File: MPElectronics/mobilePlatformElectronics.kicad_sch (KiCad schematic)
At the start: 92 parts, among them J1 UART, J2 UART, J3 Magnetic Encoder, J4 Magnetic Encoder, M1 Motor_DC, M2 Motor_DC, M3 Motor_DC, M4 Motor_DC, M5 SG90 9g Micro Servo, M6 RDS51150, M7 RDS51150, M8 SY35ST28-0504A_Stepper_Motor_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, Q1 LTR3208E, SW1 Reset, SW2 Reset, SW3 Reset, SW4 SW_SPDT, SW5 SW_SPDT, SW6 SW_SPDT_LIMIT, SW7 SW_SPDT_LIMIT, U1 PIC32MX170F256B, U10 TLE5206-2S, U12 IR Distance, U13 IR Distance, U14 L293NE/SN754410NE, U2 TLE5206-2S, U3 PIC32MX170F256B, U4 IR Line Sensor, U5 IR Line Sensor, U6 IR Line Sensor, U7 MCP6294, U8 LM339AN, U9 IR Line Sensor

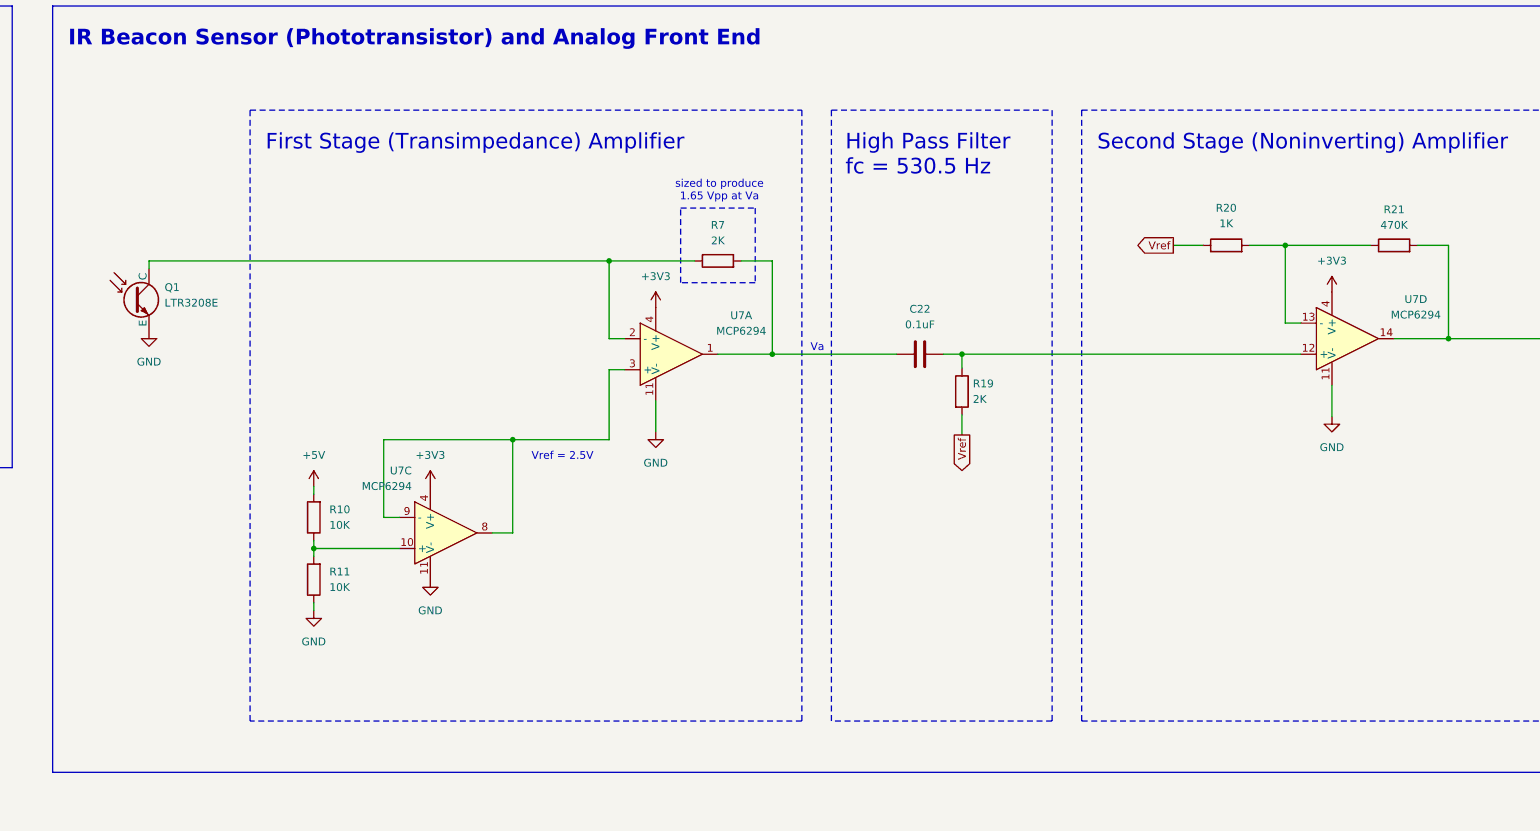
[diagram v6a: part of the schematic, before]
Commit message: changesignal conditioning vref connections and rails from 5v to 3v3
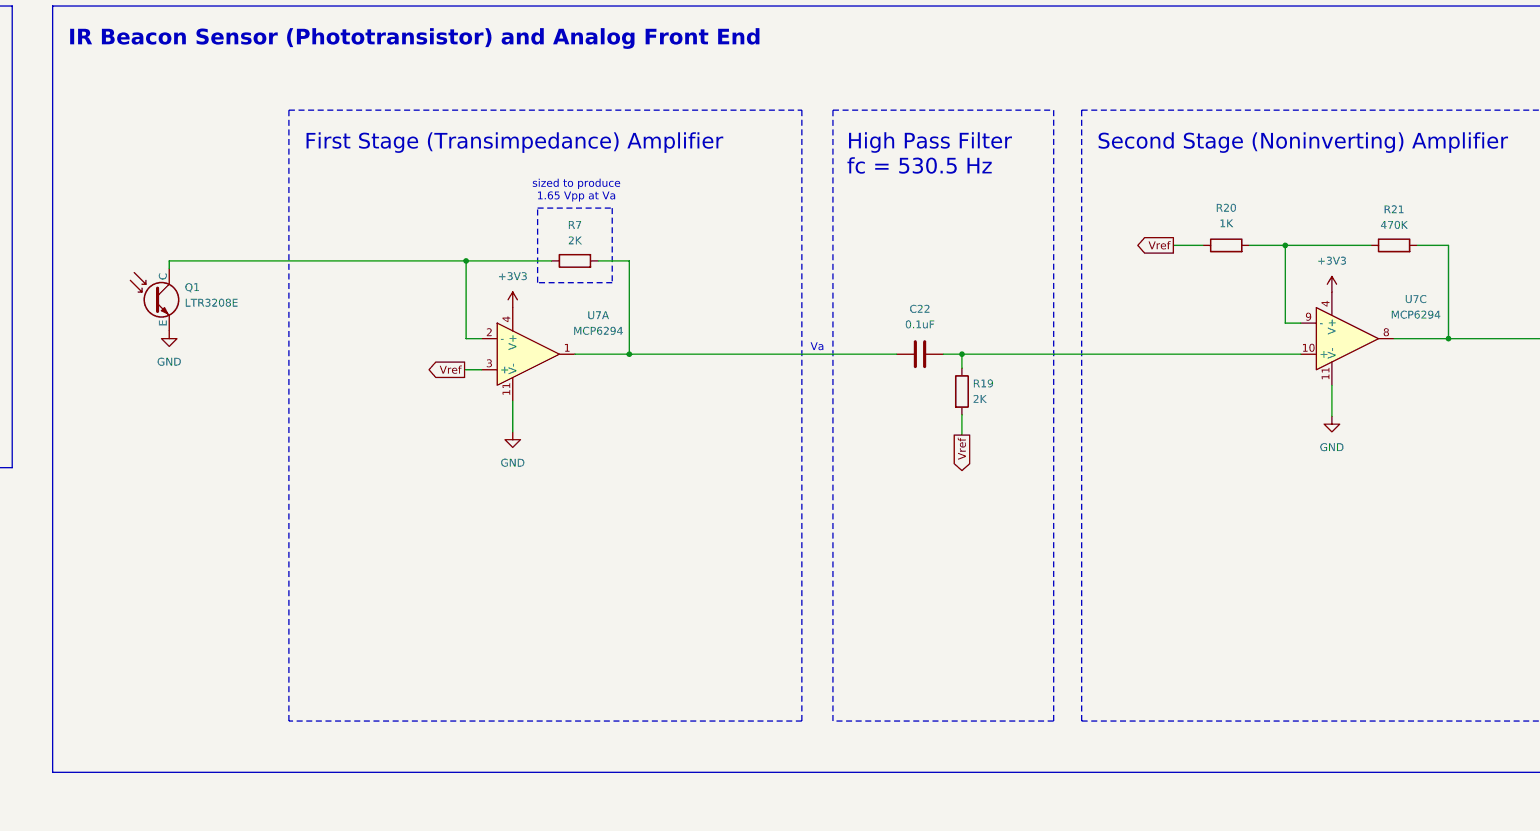
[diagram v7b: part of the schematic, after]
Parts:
- removed R10, R11: 10K, symbol ME218_BaseLib:Res2
- removed unit 3 of U7
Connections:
- net Vref: now also U7.3 (+)
- net at R20.2, R21.1: now also U7.9 (-); no longer U7.13 (-)
- net at R21.2, U8.4 (-): now also U7.8; no longer U7.14
- net at C22.1, R19.1: now also U7.10 (+); no longer U7.12 (+)
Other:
- note removed: "Vref = 2.5V"
- moved on the sheet: Q1, R7, U7A

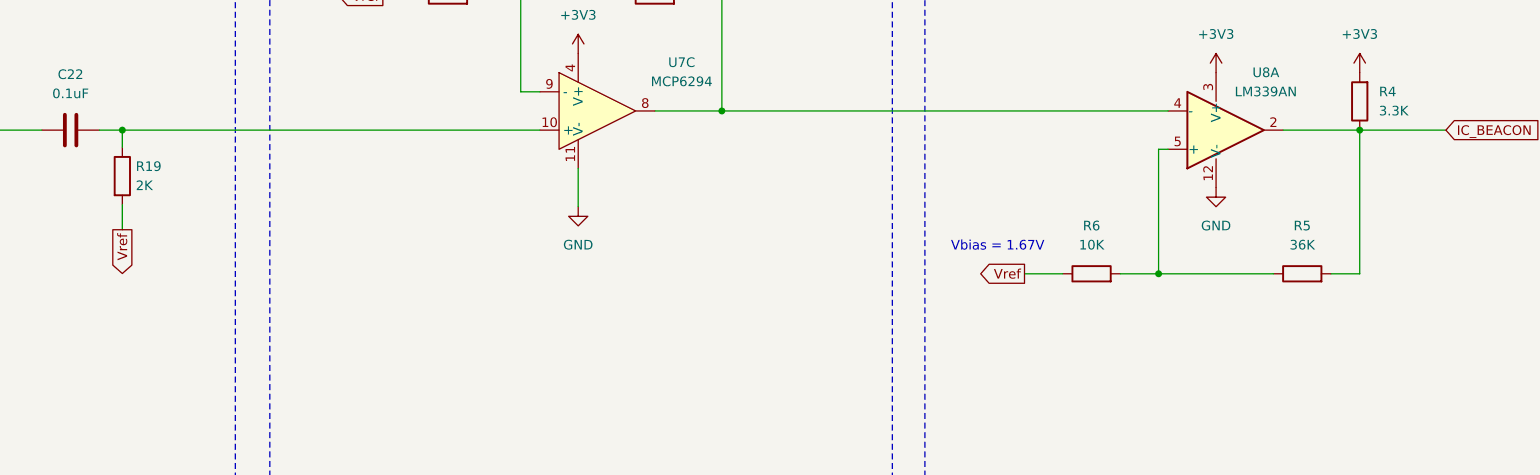
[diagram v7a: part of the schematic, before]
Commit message: schematic filter update
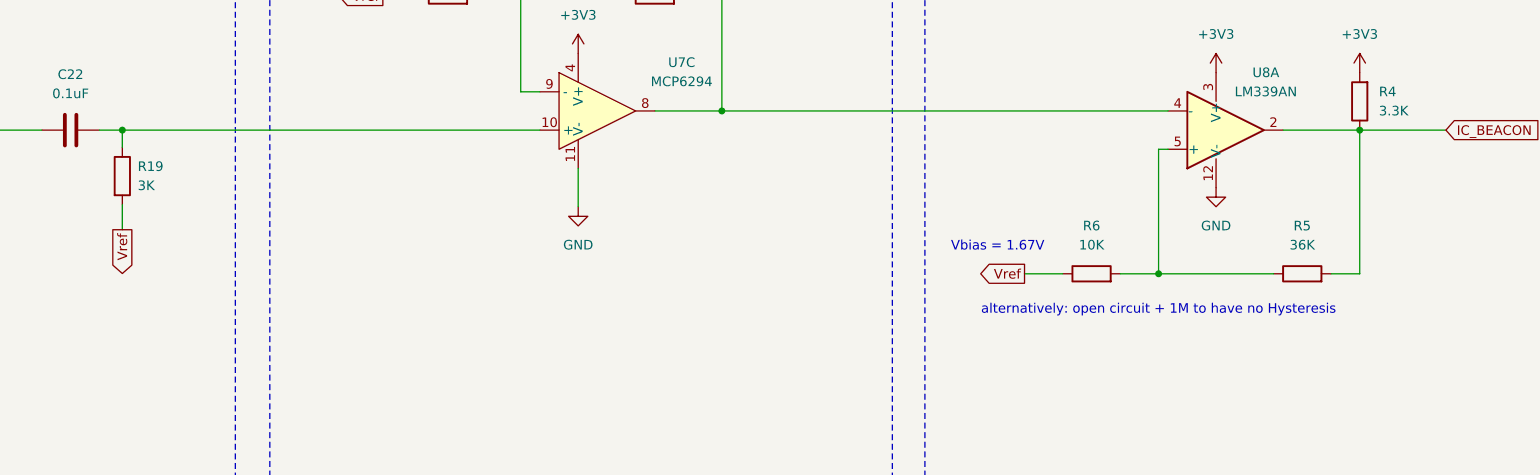
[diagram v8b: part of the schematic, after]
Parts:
- R19: value 2K -> 3K
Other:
- note added: "alternatively: open circuit + 1M to have no Hysteresis"
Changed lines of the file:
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@@
 		)
 	)
+	(text "alternatively: open circuit + 1M to have no Hysteresis"
+		(exclude_from_sim no)
+		(at 824.992 146.558 0)
+		(effects
+			(font
+				(size 1.27 1.27)
+			)
+		)
+	)
 	(text "Field Side Indicator"
 		(exclude_from_sim no)
@@
 		(fields_autoplaced yes)
 		(property "Reference" "R19"
-			(at 689.356 127.5079 0)
+			(at 689.61 127.5079 0)
 			(effects
 				(font
@@
 			)
 		)
-		(property "Value" "2K"
-			(at 689.356 130.0479 0)
+		(property "Value" "3K"
+			(at 689.61 130.0479 0)
 			(effects
 				(font
